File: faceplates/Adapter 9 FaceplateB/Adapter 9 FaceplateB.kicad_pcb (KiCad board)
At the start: 2 copper layers, 70.7 x 46.7 mm, 5 parts, among them M1 Mounting, M2 Mounting, M3 Mounting, M4 Mounting

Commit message: Tweaked for cosmetics
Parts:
- added G***: LOGO, logo:c64_joykey, B.Cu at (226.1, 118.2)
- moved G*** 0.08 mm to (226.1, 118.2)
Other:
- outline, holes or cut-outs redrawn
- board text added: "A"
- board text added: "B"
- board text added: "B1"
- board text added: "GP2040"
- board text added: "HOME"
- board text added: "L"
- board text added: "L2"
- board text added: "MENU"
- board text added: "Mini"
- board text added: "R"
- board text added: "R2"
- board text added: "SHARE"
- board text added: "X"
- board text added: "Y"

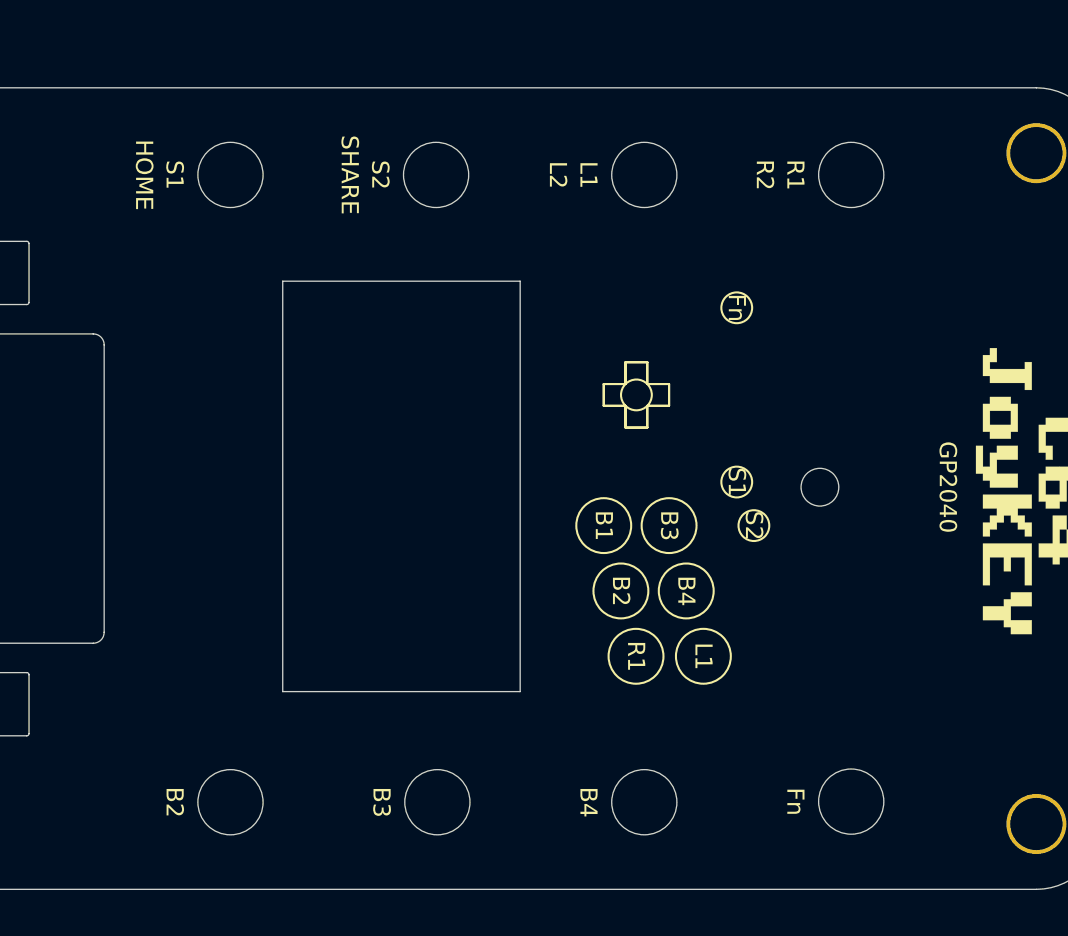
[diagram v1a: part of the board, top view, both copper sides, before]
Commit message: Larger labels
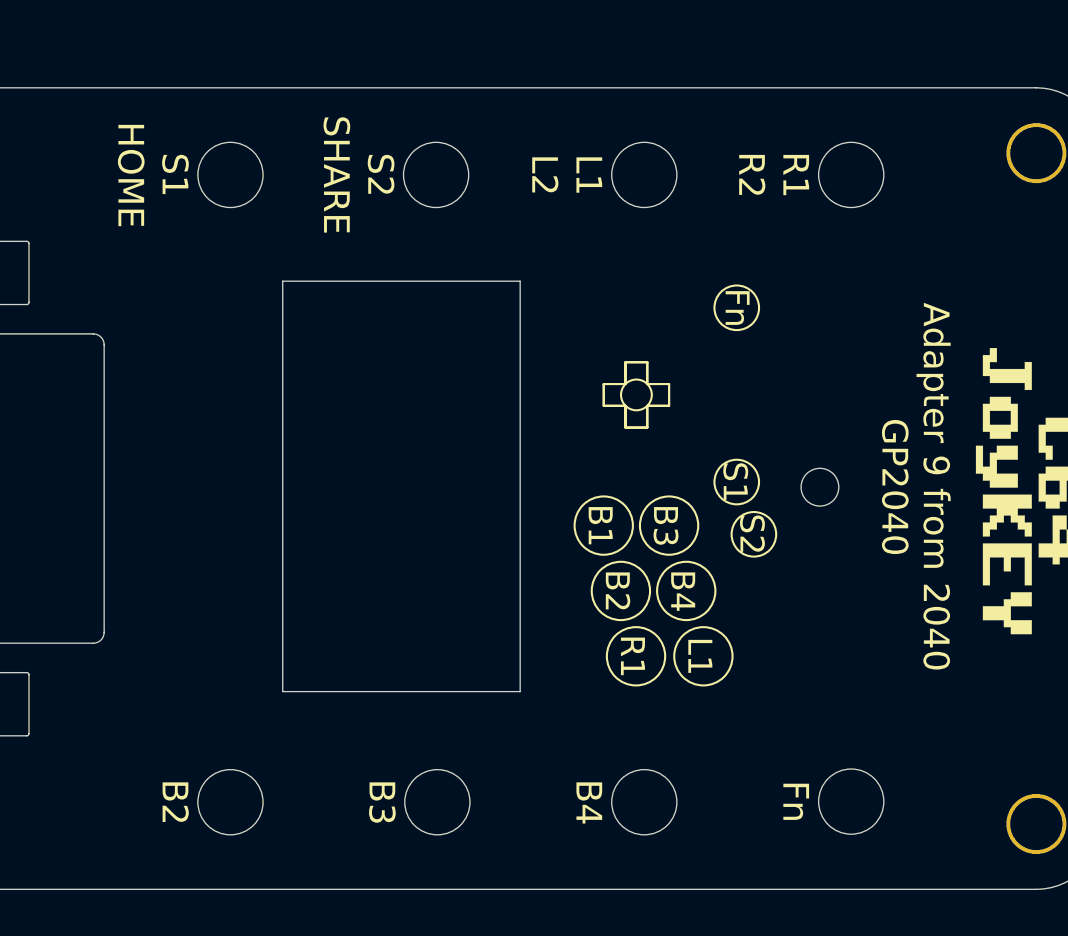
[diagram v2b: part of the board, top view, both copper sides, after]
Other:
- board text added: "Adapter 9 from 2040 GP2040"
- board text added: "Adapter 9 from 2040 {dblquote}Mini{dblquote}"
- board text removed: "GP2040"
- board text removed: "Mini"
